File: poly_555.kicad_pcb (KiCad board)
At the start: 2 copper layers, 121.9 x 177.2 mm, 155 parts, among them U1 LM386, U10 555, U11 555, U12 555, U13 555, U14 555, U2 555, U3 555, U4 555, U5 555, U6 555, U7 555, U8 555, U9 555

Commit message: Mounting holes
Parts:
- removed the S1 at (131.4, -51.4)
- added ?: MountingHole_2mm, MountingHole:MountingHole_2mm, F.Cu at (34.3, 181.6)
- added ?: MountingHole_2mm, MountingHole:MountingHole_2mm, F.Cu at (90.2, 181.6)
- added ?: MountingHole_2mm, MountingHole:MountingHole_2mm, F.Cu at (146.1, 181.6)
- added ?: MountingHole_2mm, MountingHole:MountingHole_2mm, F.Cu at (90.2, 157.5)
- added ?: MountingHole_2mm, MountingHole:MountingHole_2mm, F.Cu at (146.1, 157.5)
- added ?: MountingHole_2mm, MountingHole:MountingHole_2mm, F.Cu at (34.3, 157.5)
- added ?: MountingHole_2mm, MountingHole:MountingHole_2mm, F.Cu at (146.1, 31.8)
- added ?: MountingHole_2mm, MountingHole:MountingHole_2mm, F.Cu at (34.3, 31.8)
- R1: footprint Resistor_THT:R_Axial_DIN0204_L3.6mm_D1.6mm_P7.62mm_Horizontal -> Resistor_THT:R_Axial_DIN0207_L6.3mm_D2.5mm_P2.54mm_Vertical
- RV1: footprint Potentiometer_THT:Potentiometer_Alpha_RD901F-40-00D_Single_Vertical -> Potentiometer_THT:Potentiometer_Bourns_3386F_Vertical
- RV2: value R_POT_TRIM_US -> FINE
- RV3: value R_POT_TRIM_US -> COURSE
- moved BT1 169.1 mm to (146.1, 113.0), turned to 180 degrees
- moved D1 112.0 mm to (137.2, 110.5)
- moved R1 111.5 mm to (137.2, 115.6)
- moved R2 72.7 mm to (136.5, 52.7)
- moved RV1 72.5 mm to (142.9, 48.3)
- moved C2 66.1 mm to (115.7, 103.9), turned to 0 degrees
- moved C11 66.0 mm to (82.4, 80.6)
- moved C13 66.0 mm to (86.7, 33.0)
- moved C18 66.0 mm to (97.8, 69.2)
- moved C19 66.0 mm to (118.7, 33.0)
- moved C26 66.0 mm to (50.8, 144.1)
- moved C27 66.0 mm to (34.3, 132.7)
- moved C28 66.0 mm to (55.2, 97.2)
- moved C30 66.0 mm to (43.8, 101.0)
- moved C32 66.0 mm to (82.5, 144.1)
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- renumbered S2 to S1, S11 to S10, S12 to S11, S13 to S12, S14 to S13, S3 to S2, S4 to S3, S5 to S4, S6 to S5, S7 to S6, S8 to S7, S9 to S8, S10 to S9
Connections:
- R1 pad 1: Net-(R1-Pad1) -> Net-(BT1-Pad1)
- S1 pad 1: Net-(R1-Pad1) -> Net-(BT1-Pad1)
- S1 pad 2: Net-(R1-Pad1) -> Net-(BT1-Pad1)
- S10 pad 1: Net-(R1-Pad1) -> Net-(BT1-Pad1)
- S10 pad 2: Net-(R1-Pad1) -> Net-(BT1-Pad1)
- S11 pad 1: Net-(R1-Pad1) -> Net-(BT1-Pad1)
- S11 pad 2: Net-(R1-Pad1) -> Net-(BT1-Pad1)
- S12 pad 1: Net-(R1-Pad1) -> Net-(BT1-Pad1)
- S12 pad 2: Net-(R1-Pad1) -> Net-(BT1-Pad1)
- S13 pad 1: Net-(R1-Pad1) -> Net-(BT1-Pad1)
- S13 pad 2: Net-(R1-Pad1) -> Net-(BT1-Pad1)
- S2 pad 1: Net-(R1-Pad1) -> Net-(BT1-Pad1)
- S2 pad 2: Net-(R1-Pad1) -> Net-(BT1-Pad1)
- S3 pad 1: Net-(R1-Pad1) -> Net-(BT1-Pad1)
- S3 pad 2: Net-(R1-Pad1) -> Net-(BT1-Pad1)
- S4 pad 1: Net-(R1-Pad1) -> Net-(BT1-Pad1)
- S4 pad 2: Net-(R1-Pad1) -> Net-(BT1-Pad1)
- S5 pad 1: Net-(R1-Pad1) -> Net-(BT1-Pad1)
- S5 pad 2: Net-(R1-Pad1) -> Net-(BT1-Pad1)
- S6 pad 1: Net-(R1-Pad1) -> Net-(BT1-Pad1)
- S6 pad 2: Net-(R1-Pad1) -> Net-(BT1-Pad1)
- S7 pad 1: Net-(R1-Pad1) -> Net-(BT1-Pad1)
- S7 pad 2: Net-(R1-Pad1) -> Net-(BT1-Pad1)
- S8 pad 1: Net-(R1-Pad1) -> Net-(BT1-Pad1)
- S8 pad 2: Net-(R1-Pad1) -> Net-(BT1-Pad1)
- S9 pad 1: Net-(R1-Pad1) -> Net-(BT1-Pad1)
- S9 pad 2: Net-(R1-Pad1) -> Net-(BT1-Pad1)
- U1 pad 4: Net-(R1-Pad1) -> Net-(BT1-Pad1)
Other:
- board size 121.9 x 177.2 mm -> 121.9 x 158.8 mm

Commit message: Routed, good?
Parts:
- RV1: value R_POT_TRIM_US -> VOLUME
- moved R20 7.62 mm to (125.1, 51.4), turned to 180 degrees
- moved R21 7.62 mm to (125.1, 54.0), turned to 180 degrees
- moved R23 7.62 mm to (147.3, 83.8), turned to 180 degrees
- moved R24 7.62 mm to (147.3, 86.4), turned to 180 degrees
- moved R35 7.62 mm to (93.3, 115.6), turned to 180 degrees
- moved R36 7.62 mm to (93.3, 118.1), turned to 180 degrees
- moved R41 7.62 mm to (147.3, 147.3), turned to 180 degrees
- moved R42 7.62 mm to (147.3, 149.9), turned to 180 degrees
- moved R26 7.62 mm to (52.1, 147.3), turned to 180 degrees
- moved R27 7.62 mm to (52.1, 149.9), turned to 180 degrees
- moved R29 7.62 mm to (61.6, 115.6), turned to 180 degrees
- moved R30 7.62 mm to (61.6, 118.1), turned to 180 degrees
- moved R5 7.62 mm to (52.1, 83.8), turned to 180 degrees
- moved R6 7.62 mm to (52.1, 86.4), turned to 180 degrees
- moved R8 7.62 mm to (61.4, 52.1), turned to 180 degrees
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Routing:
- net GND: track 0.00 -> 959.8 mm, vias 0 -> 8
- net /555_astable/Out: track 0.00 -> 456.4 mm, vias 0 -> 6
- net Net-(BT1-Pad1): track 0.00 -> 287.0 mm
- net /sheet5EF2302B/9v: track 0.00 -> 197.8 mm
- net /sheet5EF259DC/9v: track 0.00 -> 185.9 mm
- net /sheet5EF2B20E/9v: track 0.00 -> 181.2 mm, vias 0 -> 2
- net /sheet5EF60550/9v: track 0.00 -> 178.3 mm
- net /sheet5EF17814/9v: track 0.00 -> 168.8 mm
- net /sheet5EF27E47/9v: track 0.00 -> 154.3 mm
- net /555_astable/9v: track 0.00 -> 141.0 mm
- net /sheet5EF60552/9v: track 0.00 -> 124.5 mm
- net /sheet5EF60554/9v: track 0.00 -> 120.0 mm
- net /sheet5EF60551/9v: track 0.00 -> 98.6 mm
- net /sheet5EF60553/9v: track 0.00 -> 82.1 mm
- net /sheet5EF60555/9v: track 0.00 -> 73.0 mm
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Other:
- board text added: "-"
- board text added: "OSKITONE POLY_555 0.0.0"

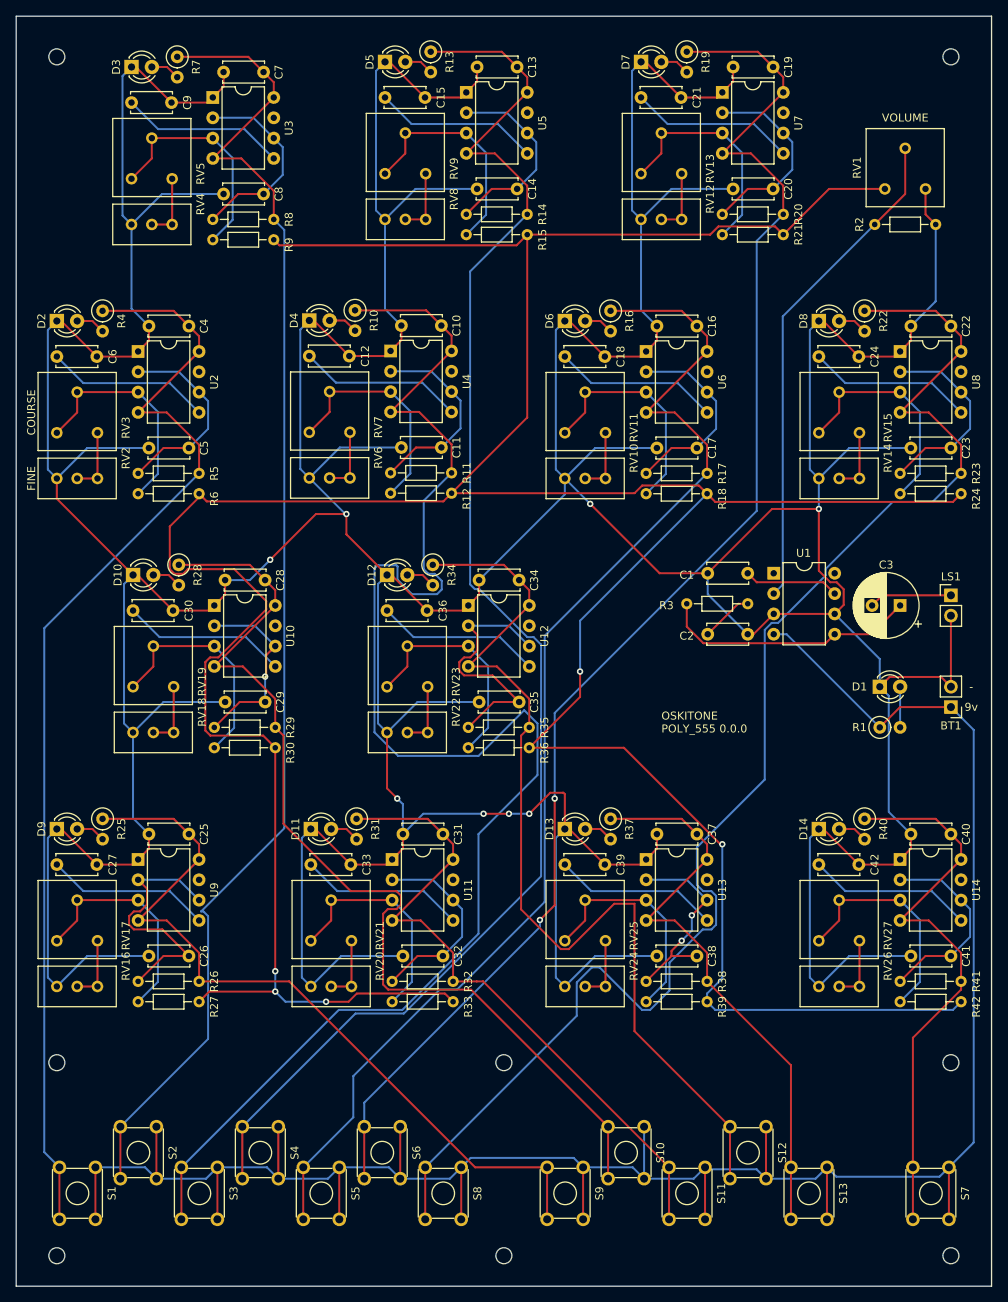
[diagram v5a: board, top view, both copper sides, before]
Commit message: Smaller, routed, close to good
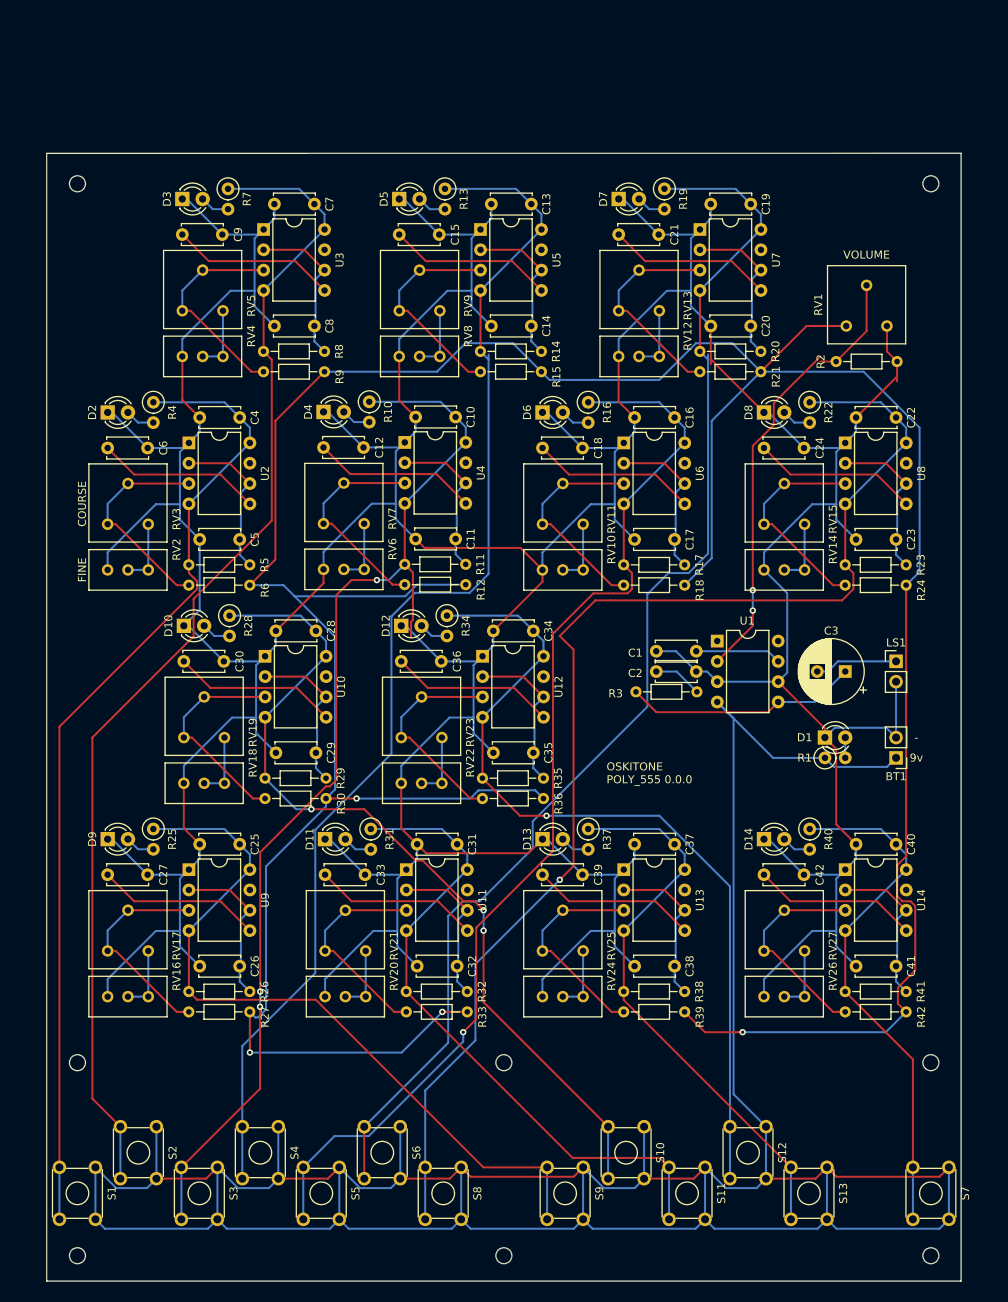
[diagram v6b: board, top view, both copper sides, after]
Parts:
- removed the ? at (146.1, 181.6)
- removed the ? at (146.1, 157.5)
- removed the ? at (34.3, 157.5)
- removed the ? at (146.1, 31.8)
- added ?: MountingHole_2mm, MountingHole:MountingHole_2mm, F.Cu at (143.5, 181.6)
- added ?: MountingHole_2mm, MountingHole:MountingHole_2mm, F.Cu at (143.5, 157.5)
- added ?: MountingHole_2mm, MountingHole:MountingHole_2mm, F.Cu at (36.9, 157.5)
- added ?: MountingHole_2mm, MountingHole:MountingHole_2mm, F.Cu at (143.5, 47.6)
- moved R20 20.1 mm to (114.7, 68.6), turned to 0 degrees
- moved R23 18.5 mm to (132.8, 95.2), turned to 0 degrees
- moved R14 18.1 mm to (87.2, 68.6), turned to 0 degrees
- moved R2 17.8 mm to (131.7, 69.8)
- moved RV1 17.8 mm to (138.0, 65.4)
- moved C9 17.7 mm to (50.0, 54.0)
- moved D3 17.7 mm to (50.0, 49.5)
- moved R7 17.7 mm to (55.7, 48.2)
- moved RV4 17.7 mm to (50.0, 69.2)
- moved U3 17.7 mm to (60.1, 53.3)
- moved C7 17.7 mm to (66.5, 50.2)
- moved RV5 17.7 mm to (55.1, 63.5)
- moved C8 17.7 mm to (66.5, 65.4)
- moved R9 17.7 mm to (67.7, 71.1)
- moved R21 17.4 mm to (122.3, 71.1)
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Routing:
- net GND: track 959.8 -> 774.9 mm, vias 8 -> 0
- net Net-(BT1-Pad1): track 287.0 -> 399.2 mm
- net /sheet5EF2302B/9v: track 197.8 -> 139.8 mm, vias 0 -> 3
- net /555_astable/Out: track 456.4 -> 415.7 mm, vias 6 -> 4
- net /sheet5EF259DC/9v: track 185.9 -> 154.9 mm
- net /sheet5EF2B20E/9v: track 181.2 -> 158.7 mm, vias 2 -> 0
- net /sheet5EF60550/9v: track 178.3 -> 157.6 mm, vias 0 -> 1
- net /sheet5EF17814/9v: track 168.8 -> 148.2 mm
- net /sheet5EF60552/9v: track 124.5 -> 107.8 mm, vias 0 -> 3
- net /sheet5EF27E47/9v: track 154.3 -> 138.0 mm, vias 0 -> 1
- net /sheet5EF60554/9v: track 120.0 -> 106.8 mm, vias 0 -> 1
- net Net-(C35-Pad1): track 32.9 -> 19.9 mm
- net Net-(C26-Pad1): track 32.9 -> 19.9 mm
- net /555_astable/9v: track 141.0 -> 130.7 mm
- net Net-(R2-Pad1): track 62.5 -> 56.5 mm, vias 0 -> 2
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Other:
- board size 121.9 x 158.8 mm -> 114.3 x 141 mm
- rule pad_to_mask_clearance: 0.05 -> 0.0508

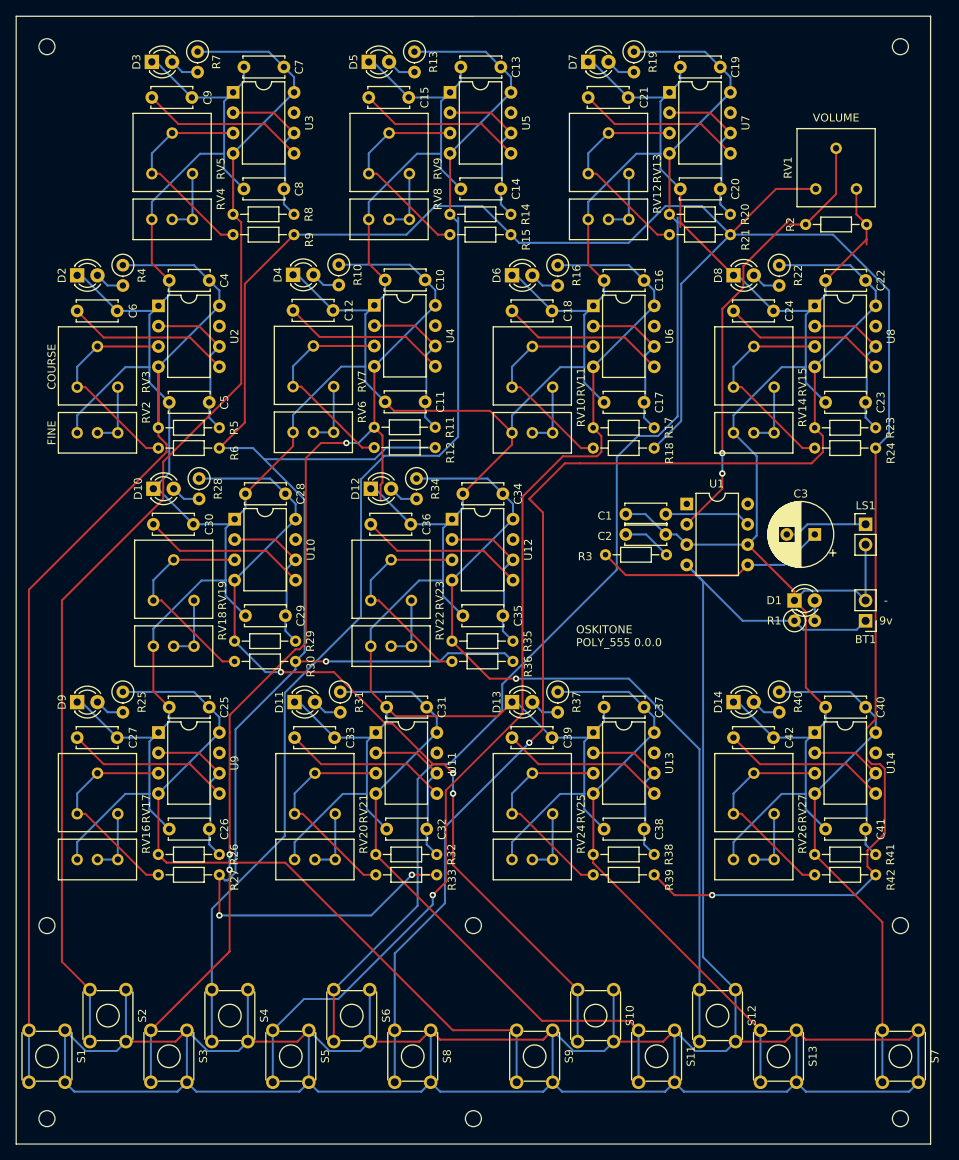
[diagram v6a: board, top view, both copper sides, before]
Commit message: Fix hole diam, unconnected R2
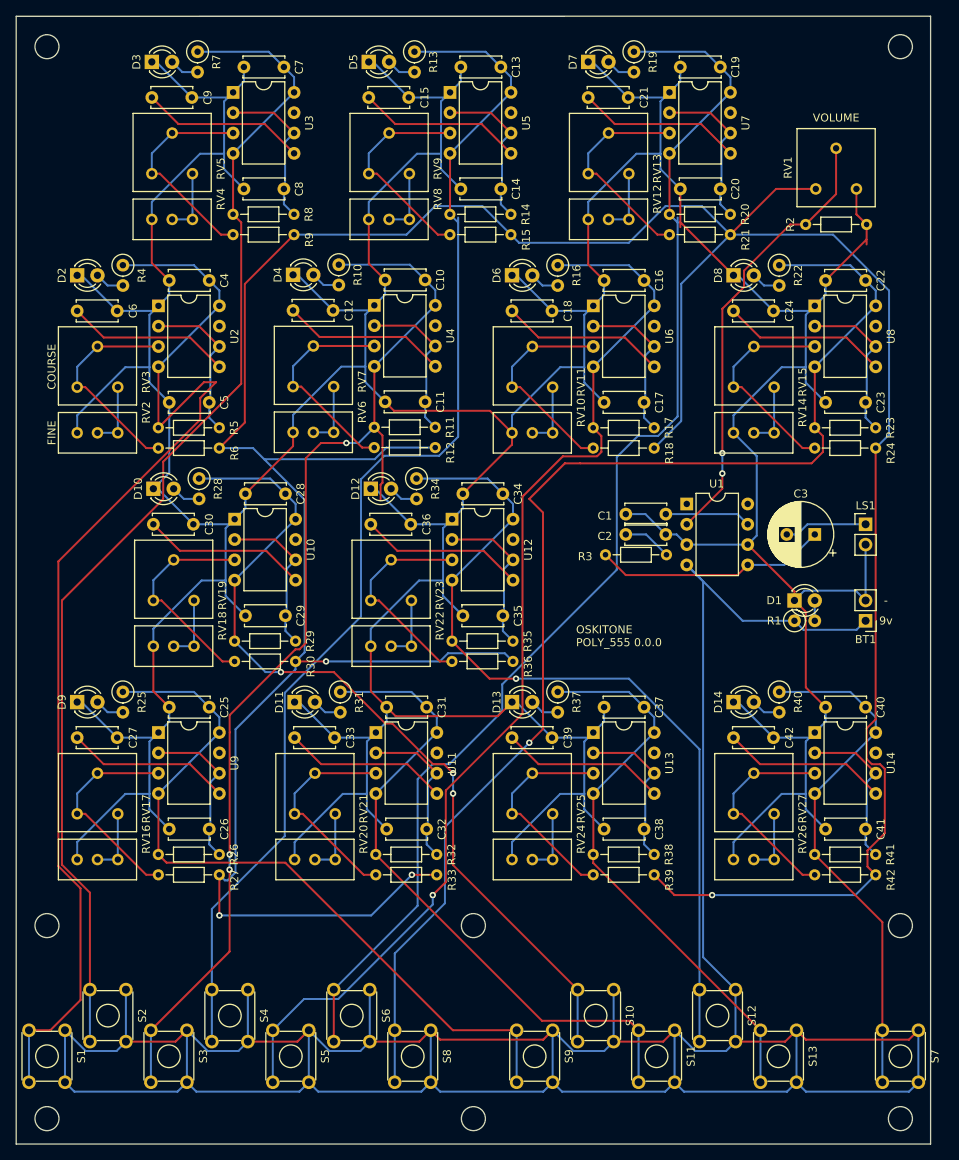
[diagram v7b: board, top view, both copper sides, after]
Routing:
- net /555_astable/9v: track 130.7 -> 144.3 mm
- net Net-(R2-Pad1): track 56.5 -> 55.9 mm
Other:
- board text added: "TODO: consider longer heel to counter key presses"

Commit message: Rerouting after footpring changes
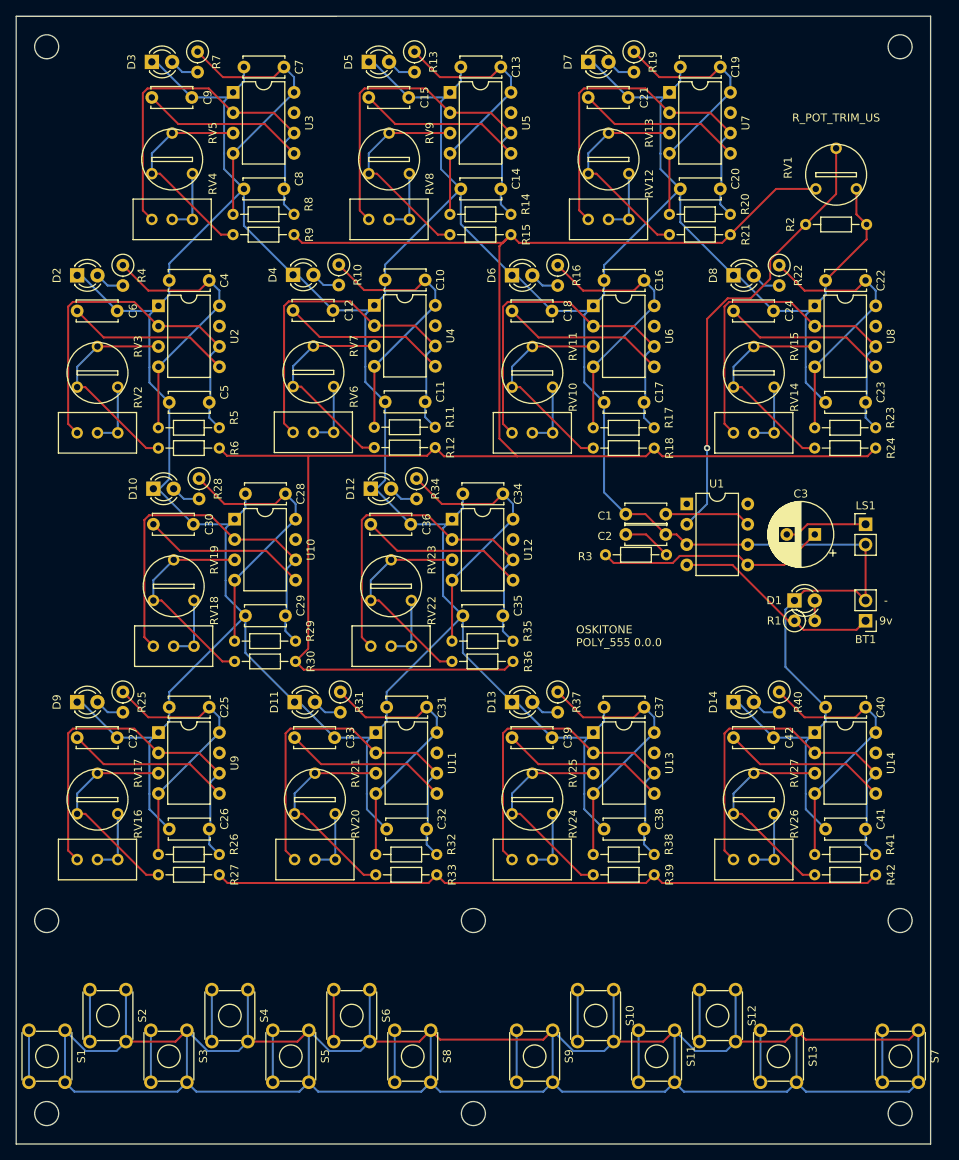
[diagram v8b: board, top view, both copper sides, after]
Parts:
- removed ? (x8): MountingHole_2mm, MountingHole:MountingHole_2mm
- added REF**: MountingHole_3.2mm_M3, MountingHole:MountingHole_3.2mm_M3, F.Cu at (36.8, 156.8)
- added REF**: MountingHole_3.2mm_M3, MountingHole:MountingHole_3.2mm_M3, F.Cu at (90.2, 156.8)
- added REF**: MountingHole_3.2mm_M3, MountingHole:MountingHole_3.2mm_M3, F.Cu at (143.5, 156.8)
- added REF**: MountingHole_3.2mm_M3, MountingHole:MountingHole_3.2mm_M3, F.Cu at (90.2, 181.0)
- added REF**: MountingHole_3.2mm_M3, MountingHole:MountingHole_3.2mm_M3, F.Cu at (143.5, 181.0)
- added REF**: MountingHole_3.2mm_M3, MountingHole:MountingHole_3.2mm_M3, F.Cu at (36.8, 181.0)
- added REF**: MountingHole_3.2mm_M3, MountingHole:MountingHole_3.2mm_M3, F.Cu at (143.5, 47.6)
- added REF**: MountingHole_3.2mm_M3, MountingHole:MountingHole_3.2mm_M3, F.Cu at (36.8, 47.6)
- C11, C14, C17, C20, C23, C26, C29, C32, C35, C38, C41, C5, C8: value C -> 10pF
- RV1: value VOLUME -> R_POT_TRIM_US; footprint Potentiometer_THT:Potentiometer_Bourns_3386F_Vertical -> Potentiometer_THT:CUSTOM_Potentiometer_Bourns_3386F_Vertical
- RV10, RV12, RV14, RV16, RV18, RV20, RV22, RV24, RV26, RV4, RV6, RV8: value R_POT_TRIM_US -> 10k
- RV11, RV13, RV15, RV17, RV19, RV21, RV23, RV25, RV27, RV5, RV7, RV9: value R_POT_TRIM_US -> 10k; footprint Potentiometer_THT:Potentiometer_Bourns_3386F_Vertical -> Potentiometer_THT:CUSTOM_Potentiometer_Bourns_3386F_Vertical
- RV2: value FINE -> 10k
- RV3: value COURSE -> 10k; footprint Potentiometer_THT:Potentiometer_Bourns_3386F_Vertical -> Potentiometer_THT:CUSTOM_Potentiometer_Bourns_3386F_Vertical
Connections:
- RV10 pad 1: GND -> Net-(C17-Pad1)
- RV12 pad 1: GND -> Net-(C20-Pad1)
- RV14 pad 1: GND -> Net-(C23-Pad1)
- RV16 pad 1: GND -> Net-(C26-Pad1)
- RV18 pad 1: GND -> Net-(C29-Pad1)
- RV2 pad 1: GND -> Net-(C5-Pad1)
- RV20 pad 1: GND -> Net-(C32-Pad1)
- RV22 pad 1: GND -> Net-(C35-Pad1)
- RV24 pad 1: GND -> Net-(C38-Pad1)
- RV26 pad 1: GND -> Net-(C41-Pad1)
- RV4 pad 1: GND -> Net-(C8-Pad1)
- RV6 pad 1: GND -> Net-(C11-Pad1)
- RV8 pad 1: GND -> Net-(C14-Pad1)
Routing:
- net GND: track 774.9 -> 645.5 mm
- net /sheet5EF2B20E/9v: track 158.7 -> 41.2 mm
- net /sheet5EF60550/9v: track 157.6 -> 41.2 mm, vias 1 -> 0
- net /sheet5EF259DC/9v: track 154.9 -> 41.2 mm
- net /sheet5EF17814/9v: track 148.2 -> 41.2 mm
- net /555_astable/9v: track 144.3 -> 41.2 mm
- net /sheet5EF2302B/9v: track 139.8 -> 41.2 mm, vias 3 -> 0
- net /sheet5EF27E47/9v: track 138.0 -> 41.2 mm, vias 1 -> 0
- net /555_astable/Out: track 415.7 -> 322.1 mm, vias 4 -> 0
- net /sheet5EF60552/9v: track 107.8 -> 41.2 mm, vias 3 -> 0
- net /sheet5EF60554/9v: track 106.8 -> 41.2 mm, vias 1 -> 0
- net Net-(BT1-Pad1): track 399.2 -> 343.5 mm
- net /sheet5EF60551/9v: track 94.1 -> 41.2 mm
- net /sheet5EF60553/9v: track 82.1 -> 41.2 mm
- net /sheet5EF60555/9v: track 70.8 -> 41.2 mm
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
